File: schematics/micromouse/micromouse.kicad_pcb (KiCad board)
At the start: 2 copper layers, 80 x 100 mm, 13 parts, among them J1 TOF_FRONT, J2 TOF_LEFT, J3 TOF_RIGHT, J4 Conn_01x06, J5 BatteryConnector, U1 STM32F103CBTx, U2 PMW3360DM-T2QU, U3 BMI160, Y1 Crystal

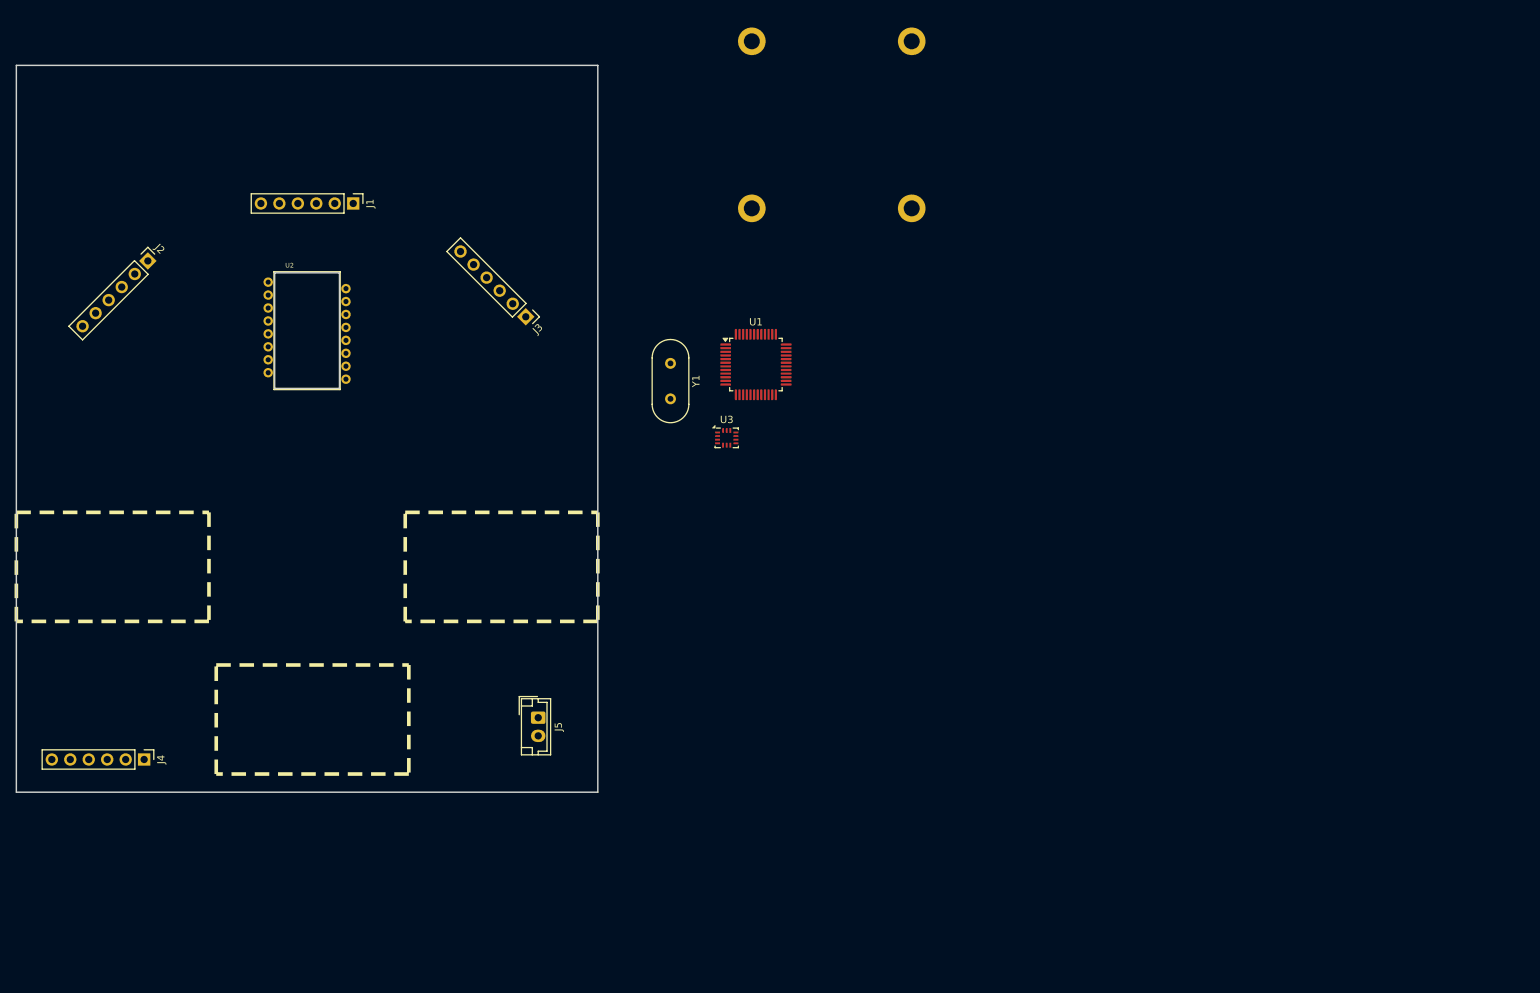
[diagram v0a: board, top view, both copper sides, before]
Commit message: Move datasheets, add application note for smt32f103 hardware development Add PCB cut from 3D model (DXF) Reorganize datasheet, add labels and connectors for tofs i2c (x2), add I2C expancer (PCF8574), add mouse sensor (PMW3360) connector and SPI1 labels Added SPI2 labels (may be removed if not used)
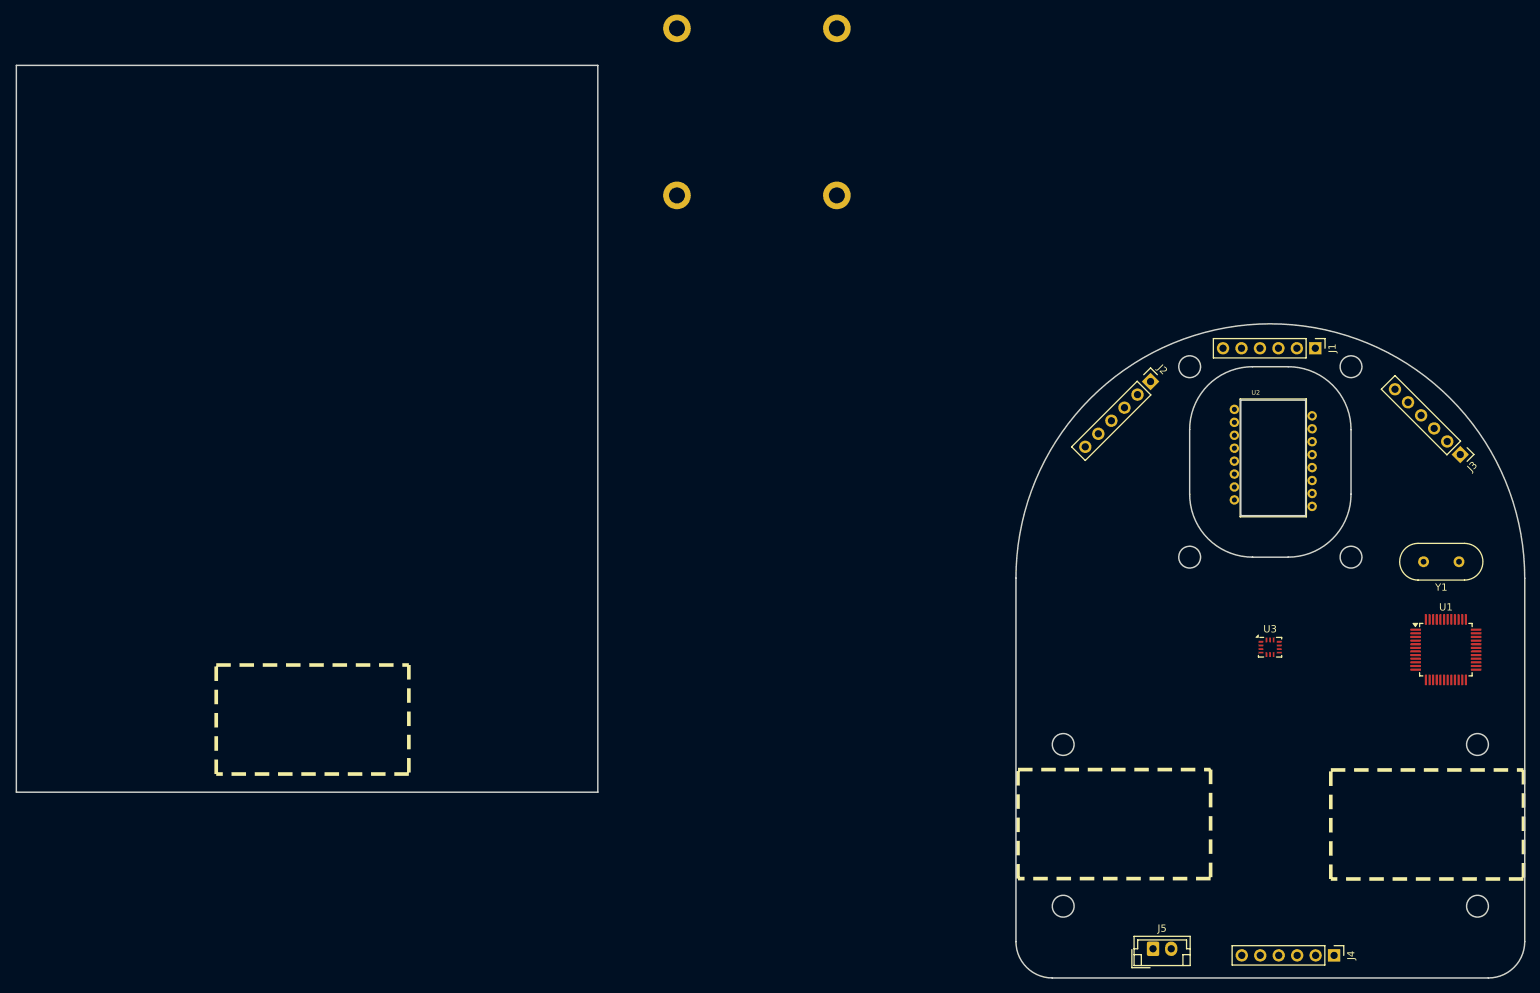
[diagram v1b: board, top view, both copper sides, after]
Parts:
- moved J4 165.9 mm to (218.8, 147.4)
- moved J2 139.0 mm to (193.5, 68.5)
- moved U2 134.1 mm to (210.4, 79.0)
- moved J1 133.9 mm to (216.2, 63.9)
- moved J3 130.0 mm to (236.2, 78.5)
- moved Y1 111.9 mm to (236.0, 93.3), turned to 180 degrees
- moved U1 102.7 mm to (234.2, 105.4)
- moved J5 90.4 mm to (193.9, 146.5), turned to 0 degrees
- moved U3 80.1 mm to (210.0, 105.1)
- moved H1 10.5 mm to (128.4, 42.9)
- moved H1 10.5 mm to (128.4, 19.9)
- moved H1 10.5 mm to (150.4, 19.9)
- moved H1 10.5 mm to (150.4, 42.9)
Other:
- board size 80 x 100 mm -> 207.5 x 125.6 mm

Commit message: Reorganize again... add things
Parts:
- removed the H1 at (128.4, 42.9)
- removed the H1 at (128.4, 19.9)
- removed the H1 at (150.4, 19.9)
- removed the H1 at (150.4, 42.9)
- removed U3: BMI160, Package_LGA:Bosch_LGA-14_3x2.5mm_P0.5mm
- added C1: C, Capacitor_SMD:C_0805_2012Metric_Pad1.18x1.45mm_HandSolder, F.Cu at (162.6, 69.4)
- added C2: C, Capacitor_SMD:C_0805_2012Metric_Pad1.18x1.45mm_HandSolder, F.Cu at (162.6, 65.2)
- added H1: MountingHole_Pad, MountingHole:MountingHole_2.2mm_M2_ISO14580_Pad, F.Cu at (127.3, 45.8)
- added H2: MountingHole_Pad, MountingHole:MountingHole_2.2mm_M2_ISO14580_Pad, F.Cu at (149.5, 45.8)
- added H3: MountingHole_Pad, MountingHole:MountingHole_2.2mm_M2_ISO14580_Pad, F.Cu at (127.3, 72.0)
- added H4: MountingHole_Pad, MountingHole:MountingHole_2.2mm_M2_ISO14580_Pad, F.Cu at (149.5, 72.0)
- added J10: MotorB_Conn, Connector_JST:JST_EH_B2B-EH-A_1x02_P2.50mm_Vertical, F.Cu at (145.6, 102.0)
- added J11: BMI_ConnB, Connector_PinHeader_2.54mm:PinHeader_1x07_P2.54mm_Vertical, F.Cu at (109.0, 46.0)
- added J12: BMI_ConnA, Connector_PinHeader_2.54mm:PinHeader_1x05_P2.54mm_Vertical, F.Cu at (118.8, 48.6)
- added J4: TOF_RIGHT, Connector_PinHeader_2.54mm:PinHeader_1x06_P2.54mm_Vertical, F.Cu at (150.3, 33.7)
- added J6: PMW3360_Conn, Connector_JST:JST_SH_BM08B-SRSS-TB_1x08-1MP_P1.00mm_Vertical, F.Cu at (119.1, 70.3)
- added J8: Programming_Conn, Connector_PinHeader_2.54mm:PinHeader_1x04_P2.54mm_Vertical, F.Cu at (155.0, 103.5)
- added J9: MotorA_Conn, Connector_JST:JST_EH_B2B-EH-A_1x02_P2.50mm_Vertical, F.Cu at (131.6, 99.5)
- added U4: PCF8574TS, Package_SO:SSOP-20_4.4x6.5mm_P0.65mm, F.Cu at (138.7, 38.4)
- J1: value TOF_FRONT -> TOF_LEFT
- J2: value TOF_LEFT -> TOF_FRONTLEFT
- J3: value TOF_RIGHT -> TOF_FRONTRIGHT
- J7: renamed from J4; value Conn_01x06 -> Bluetooth_Conn
- U2: value PMW3360DM-T2QU -> DRV8833PWP; footprint PMW3360DM:PMW3360 -> Package_SO:HTSSOP-16-1EP_4.4x5mm_P0.65mm_EP3.4x5mm_Mask2.46x2.31mm_ThermalVias
- Y1: value Crystal -> Crystal (8MHz)
- moved J1 89.9 mm to (135.4, 24.5), turned to -45 degrees
- moved J5 89.6 mm to (114.6, 104.9), turned to 90 degrees
- moved U1 86.2 mm to (163.9, 55.4), turned to 45 degrees
- moved Y1 82.6 mm to (158.6, 64.5), turned to -90 degrees
- moved J3 79.7 mm to (166.5, 39.8), turned to -90 degrees
- moved J2 76.3 mm to (122.8, 39.9), turned to -90 degrees
- moved J7 75.5 mm to (155.0, 107.2), turned to 90 degrees
- moved U2 74.9 mm to (138.7, 100.7)
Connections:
- net +3.3V renamed VCC_{3.3}
- net bt_enable renamed /BT_{enable}
- net bt_rx renamed /USART_{RX}
- net bt_state renamed /BT_{state}
- net bt_tx renamed /USART_{TX}
- J1 pad 1: tofF_xshut -> Net-(J1-Pin_1)
- J1 pad 2: tofF_int -> Net-(J1-Pin_2)
- J1 pad 3: tofF_scl -> /I2C2_{scl}
- J1 pad 4: tofF_sda -> /I2C2_{sda}
- J2 pad 1: tofL_xshut -> Net-(J2-Pin_1)
- J2 pad 2: tofL_int -> Net-(J2-Pin_2)
- J2 pad 3: tofL_scl -> /I2C2_{scl}
- J2 pad 4: tofL_sda -> /I2C2_{sda}
- J3 pad 1: tofR_xshut -> Net-(J3-Pin_1)
- J3 pad 2: tofR_int -> Net-(J3-Pin_2)
- J3 pad 3: tofR_scl -> /I2C1_{scl}
- J3 pad 4: tofR_sda -> /I2C1_{sda}
- U1 pad 15: unconnected-(U1-PA5-Pad15) -> /SPI1_{clk}
- U1 pad 16: unconnected-(U1-PA6-Pad16) -> /SPI1_{miso}
- U1 pad 17: unconnected-(U1-PA7-Pad17) -> /SPI1_{mosi}
- U1 pad 21: unconnected-(U1-PB10-Pad21) -> /I2C2_{scl}
- U1 pad 22: unconnected-(U1-PB11-Pad22) -> /I2C2_{sda}
- U1 pad 29: unconnected-(U1-PA8-Pad29) -> /PMW_{cs}
- U1 pad 30: unconnected-(U1-PA9-Pad30) -> /USART1_{TX}
- U1 pad 31: unconnected-(U1-PA10-Pad31) -> /USART1_{RX}
- U1 pad 34: unconnected-(U1-PA13-Pad34) -> /SW_{dio}
- U1 pad 37: unconnected-(U1-PA14-Pad37) -> /SW_{clk}
- U1 pad 42: unconnected-(U1-PB6-Pad42) -> /I2C1_{scl}
- U1 pad 43: unconnected-(U1-PB7-Pad43) -> /I2C1_{sda}
- U1 pad 5: unconnected-(U1-PD0-Pad5) -> Net-(U1-PD0)
- U1 pad 6: unconnected-(U1-PD1-Pad6) -> Net-(U1-PD1)
- U2 pad 1: (no net) -> /MOTOR_{sleep}
- U2 pad 10: unconnected-(U2-SCLK-Pad10) -> /MOTOR_{b2}
- U2 pad 12: unconnected-(U2-MISO-Pad12) -> VCC_{6}
- U2 pad 13: unconnected-(U2-~{CS}-Pad13) -> GND
- U2 pad 14: (no net) -> unconnected-(U2-VINT-Pad14)
- U2 pad 15: unconnected-(U2-LED_P-Pad15) -> /MOTOR_{a2}
- U2 pad 16: (no net) -> /MOTOR_{a1}
- U2 pad 2: (no net) -> Net-(J9-Pin_1)
- U2 pad 3: unconnected-(U2-VDDPIX-Pad3) -> /MOTOR_{aen}
- U2 pad 4: unconnected-(U2-VDD-Pad4) -> Net-(J9-Pin_2)
- U2 pad 5: unconnected-(U2-VDDIO-Pad5) -> Net-(J10-Pin_2)
- U2 pad 6: (no net) -> /MOTOR_{ben}
- U2 pad 7: unconnected-(U2-~{RESET}-Pad7) -> Net-(J10-Pin_1)
- U2 pad 8: unconnected-(U2-GND-Pad8) -> /MOTOR_{fault}
- U2 pad 9: unconnected-(U2-MOTION-Pad9) -> /MOTOR_{b1}
- Y1 pad 1: unconnected-(Y1-Pad1) -> Net-(U1-PD1)
- Y1 pad 2: unconnected-(Y1-Pad2) -> Net-(U1-PD0)
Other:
- board size 207.5 x 125.6 mm -> 70 x 90 mm
- board text removed: "PMW3360 PCB"

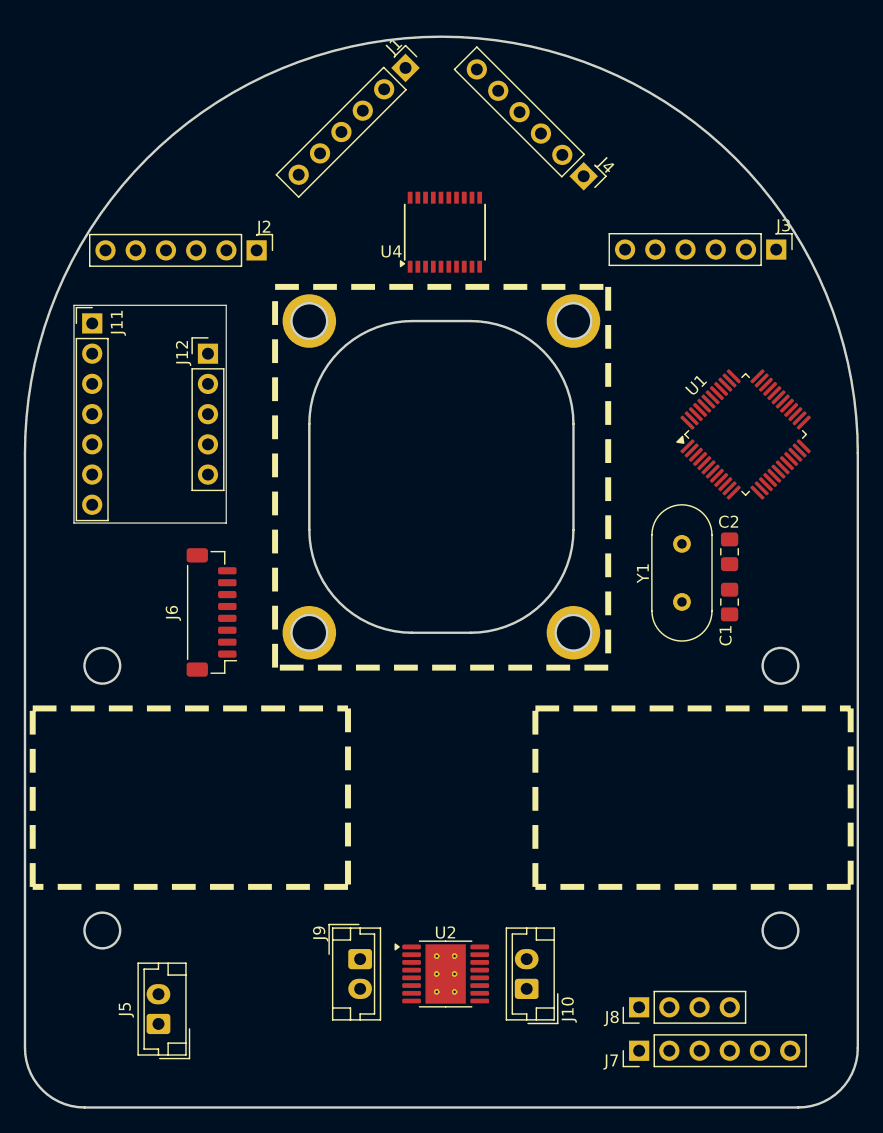
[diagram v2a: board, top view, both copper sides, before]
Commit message: Schamatic status update: * STM32 with external clock, DebugPort and communication lines (SPI1, I2C0 and I2C1) * First version of power supply schematic [TODO: Check possible short circuit] * Motor controller schematic * Mouse sensor connector + mounting holes * Bluetooth connector for HC-05/HC-06 * TOF schematic using GPIO expander * BMI160 Mounting holes
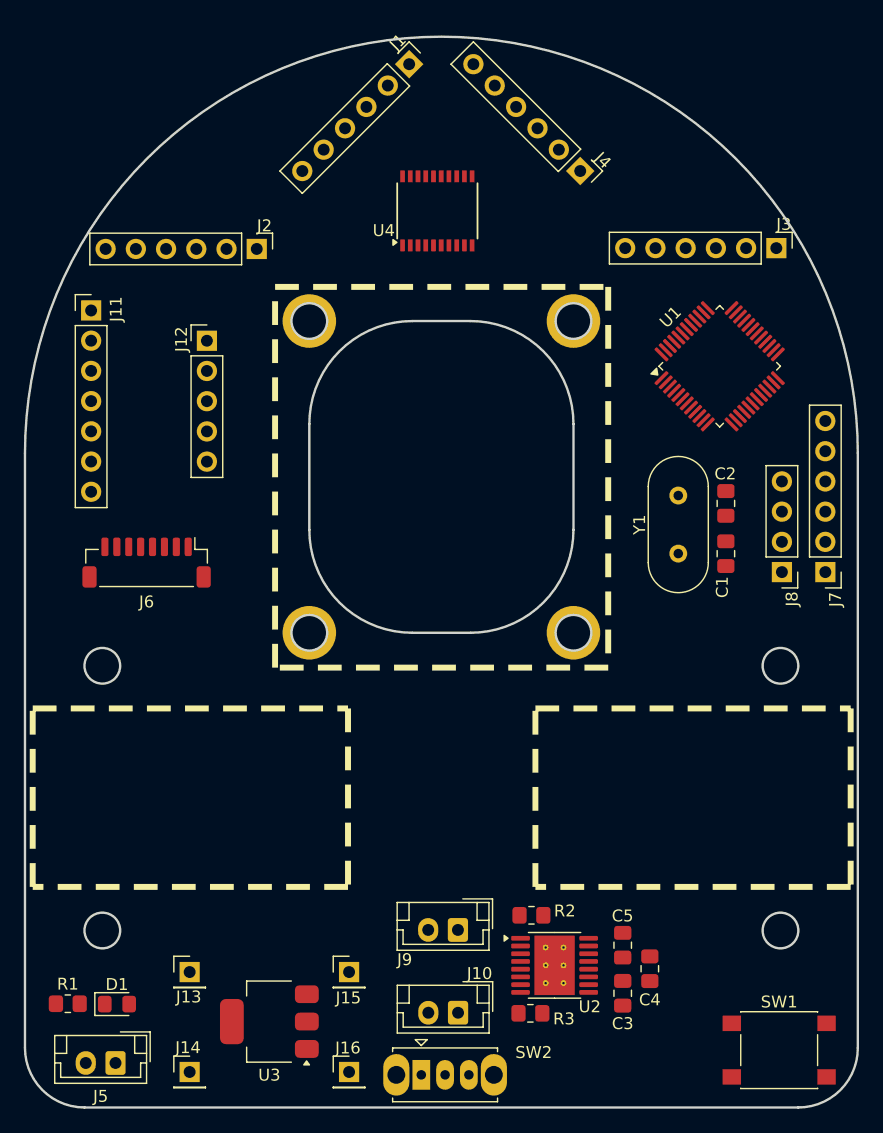
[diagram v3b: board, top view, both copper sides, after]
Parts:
- added C3: 0.01uF, Capacitor_SMD:C_0805_2012Metric_Pad1.18x1.45mm_HandSolder, F.Cu at (153.6, 102.3)
- added C4: 10uF, Capacitor_SMD:C_0805_2012Metric_Pad1.18x1.45mm_HandSolder, F.Cu at (155.9, 100.3)
- added C5: 2.2uF, Capacitor_SMD:C_0805_2012Metric_Pad1.18x1.45mm_HandSolder, F.Cu at (153.6, 98.3)
- added D1: LED, LED_SMD:LED_0805_2012Metric_Pad1.15x1.40mm_HandSolder, F.Cu at (111.1, 103.2)
- added J13: StepDown_{In+}, Connector_PinHeader_2.54mm:PinHeader_1x01_P2.54mm_Vertical, F.Cu at (117.2, 100.5)
- added J14: StepDown_{In-}, Connector_PinHeader_2.54mm:PinHeader_1x01_P2.54mm_Vertical, F.Cu at (117.2, 108.9)
- added J15: StepDown_{Out+}, Connector_PinHeader_2.54mm:PinHeader_1x01_P2.54mm_Vertical, F.Cu at (130.6, 100.5)
- added J16: StepDown_{Out-}, Connector_PinHeader_2.54mm:PinHeader_1x01_P2.54mm_Vertical, F.Cu at (130.6, 108.9)
- added R1: R, Resistor_SMD:R_0805_2012Metric_Pad1.20x1.40mm_HandSolder, F.Cu at (107.0, 103.2)
- added R2: 200m, Resistor_SMD:R_0805_2012Metric_Pad1.20x1.40mm_HandSolder, F.Cu at (145.9, 95.8)
- added R3: 200m, Resistor_SMD:R_0805_2012Metric_Pad1.20x1.40mm_HandSolder, F.Cu at (145.9, 104.0)
- added SW1: SW_Push, Button_Switch_SMD:SW_SPST_PTS645, F.Cu at (166.8, 107.1)
- added SW2: SW_SPDT, Button_Switch_THT:SW_Slide_SPDT_Straight_CK_OS102011MS2Q, F.Cu at (136.7, 109.2)
- added U3: AMS1117-3.3, Package_TO_SOT_SMD:SOT-223-3_TabPin2, F.Cu at (123.9, 104.7)
- moved J7 43.2 mm to (170.7, 66.9), turned to 180 degrees
- moved J8 38.5 mm to (167.0, 66.9), turned to 180 degrees
- moved U2 9.18 mm to (147.9, 100.0)
- moved J9 8.58 mm to (139.8, 97.0), turned to 180 degrees
- moved J6 6.88 mm to (113.6, 66.1), turned to 180 degrees
- moved U1 6.13 mm to (161.8, 49.6)
- moved J10 6.11 mm to (139.8, 104.0), turned to 180 degrees
- moved J5 4.88 mm to (111.0, 108.2), turned to 180 degrees
- moved C2 4.08 mm to (162.3, 61.1)
- moved C1 4.08 mm to (162.3, 65.4)
- moved Y1 4.08 mm to (158.3, 60.5)
- moved U4 1.90 mm to (138.0, 36.6)
- moved J11 1.09 mm to (108.9, 44.9)
- moved J12 1.09 mm to (118.7, 47.5)
- moved J4 0.53 mm to (150.0, 33.2)
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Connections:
- J5 pad 1: unconnected-(J5-Pin_1-Pad1) -> GND
- J5 pad 2: unconnected-(J5-Pin_2-Pad2) -> VCC_{7.4}
- U2 pad 11: unconnected-(U2-VCP-Pad11) -> Net-(U2-VCP)
- U2 pad 12: VCC_{6} -> VCC_{7,4}
- U2 pad 14: unconnected-(U2-VINT-Pad14) -> Net-(U2-VINT)
- U2 pad 3: /MOTOR_{aen} -> Net-(U2-AISEN)
- U2 pad 6: /MOTOR_{ben} -> Net-(U2-BISEN)
- U4 pad 5: unconnected-(U4-VDD-Pad5) -> VCC_{3.3}
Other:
- outline, holes or cut-outs redrawn
